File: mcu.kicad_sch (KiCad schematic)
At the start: 17 parts, among them CN1 FTSH-107-01-L-DV-K, U1 STM32H743VITx

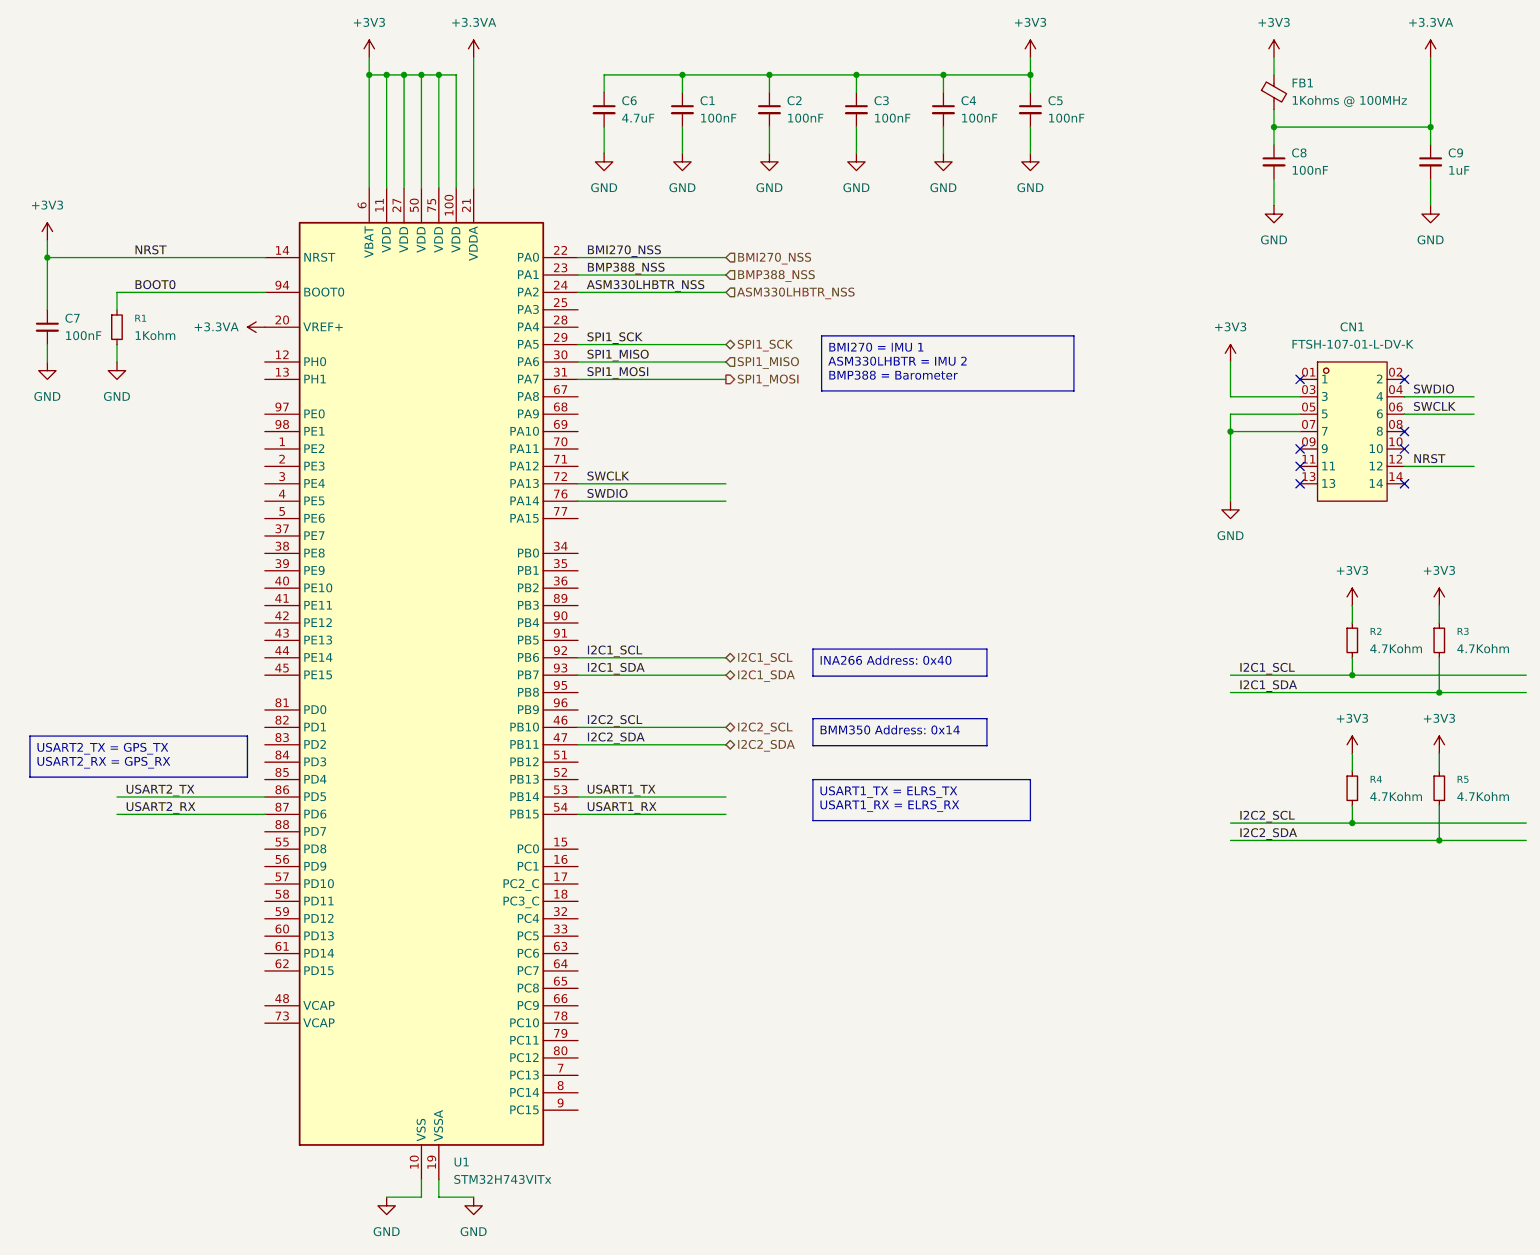
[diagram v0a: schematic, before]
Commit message: Add NavBoard connector and fix Ferrite bead for 3V3A line
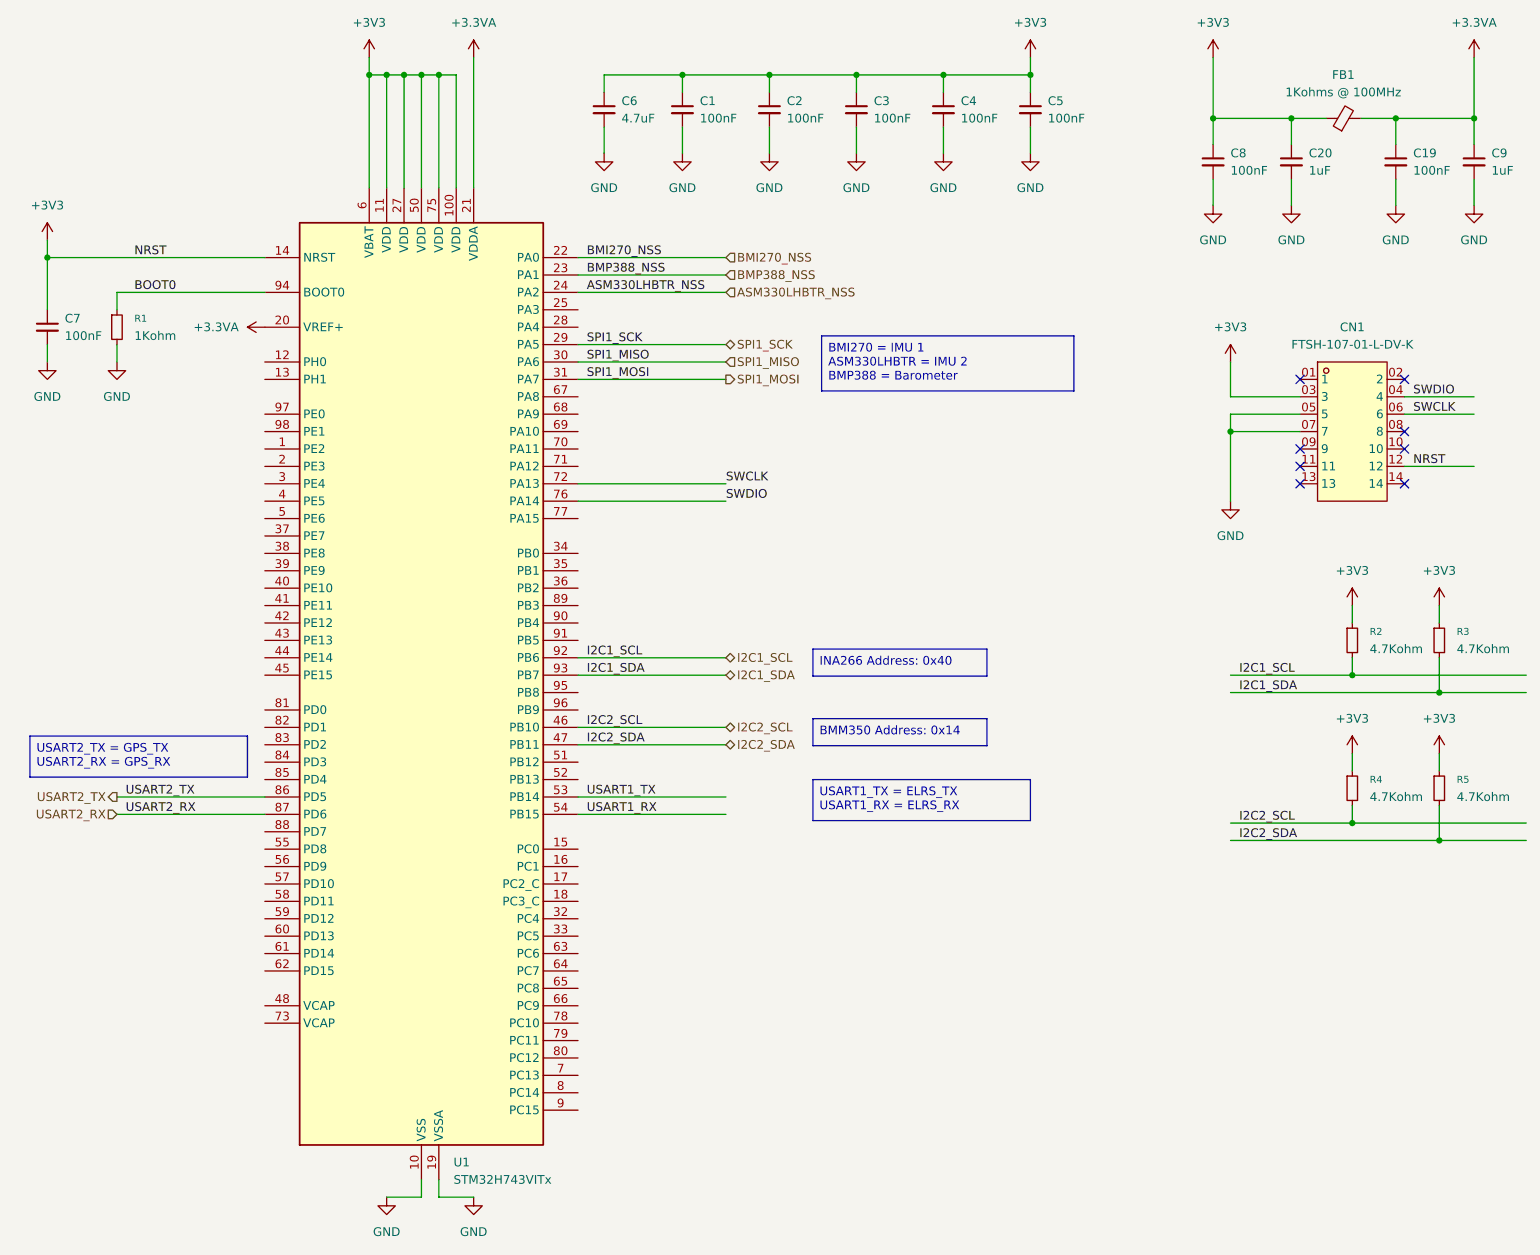
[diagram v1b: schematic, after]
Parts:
- added C19: 100nF, Capacitor_SMD:C_0201_0603Metric_Pad0.64x0.40mm_HandSolder, symbol Device:C_Small
- added C20: 1uF, Capacitor_SMD:C_0201_0603Metric_Pad0.64x0.40mm_HandSolder, symbol Device:C_Small
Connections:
- net +3.3VA: now also C19.1; no longer C8.1
- net +3V3: now also C8.1, C20.1
- net GND: now also C19.2, C20.2
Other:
- moved on the sheet: C8, C9

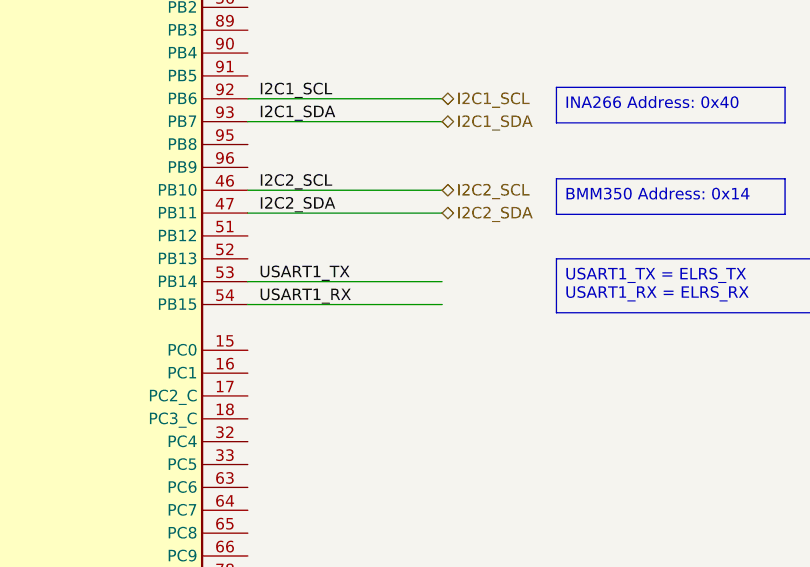
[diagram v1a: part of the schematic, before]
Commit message: added main buck to step Vbat to 5V
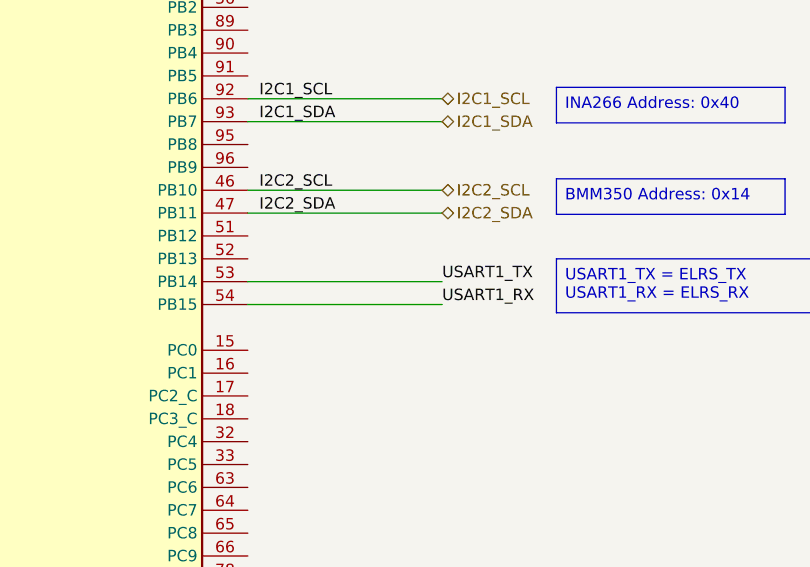
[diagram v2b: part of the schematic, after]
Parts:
- R2, R3, R4, R5: footprint (none) -> Resistor_SMD:R_0201_0603Metric
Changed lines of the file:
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@@
 	)
 	(label "USART1_TX"
-		(at 104.14 129.54 0)
+		(at 124.46 129.54 0)
 		(effects
 			(font
@@
 	)
 	(label "USART1_RX"
-		(at 104.14 132.08 0)
+		(at 124.46 132.08 0)
 		(effects
 			(font
@@
 			)
 		)
-		(property "Footprint" ""
+		(property "Footprint" "Resistor_SMD:R_0201_0603Metric"
 			(at 228.6 106.68 0)
 			(hide yes)
@@
 			)
 		)
-		(property "Footprint" ""
+		(property "Footprint" "Resistor_SMD:R_0201_0603Metric"
 			(at 215.9 106.68 0)
 			(hide yes)
@@
 			)
 		)
-		(property "Footprint" ""
+		(property "Footprint" "Resistor_SMD:R_0201_0603Metric"
 			(at 228.6 128.27 0)
 			(hide yes)
@@
 			)
 		)
-		(property "Footprint" ""
+		(property "Footprint" "Resistor_SMD:R_0201_0603Metric"
 			(at 215.9 128.27 0)
 			(hide yes)

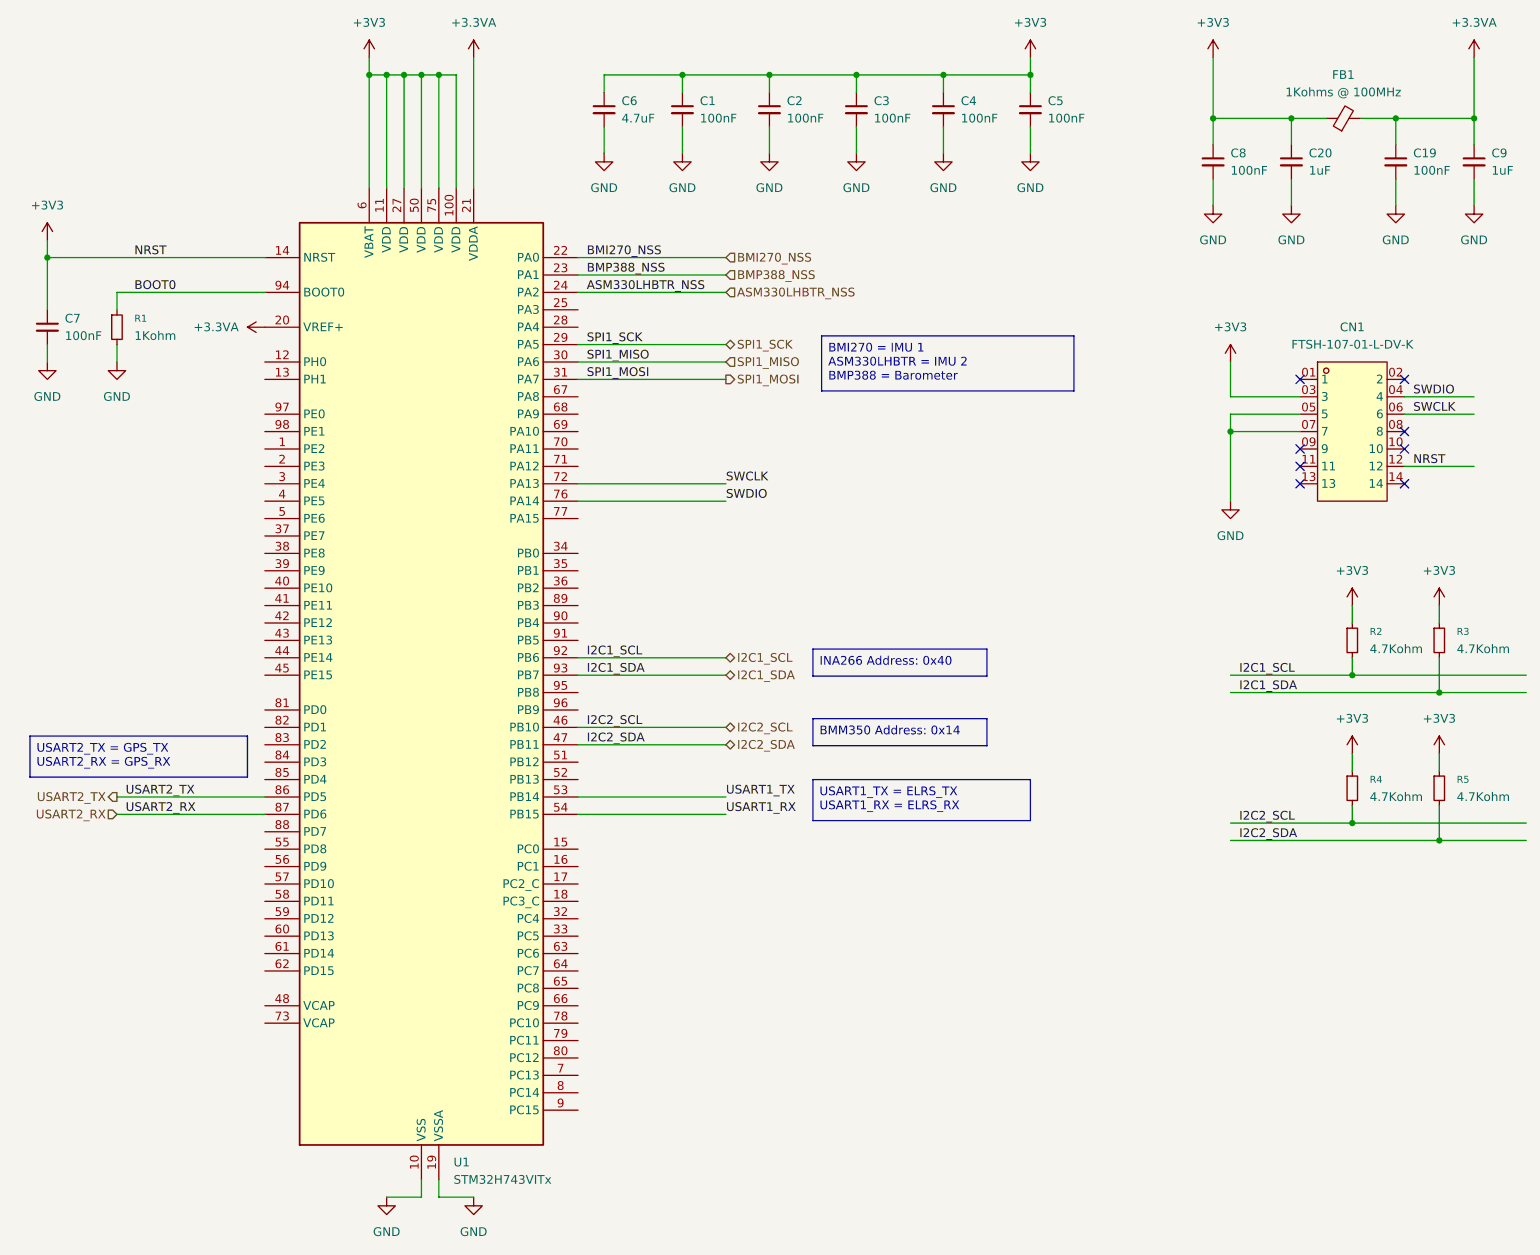
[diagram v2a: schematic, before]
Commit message: mainly added usart 3, uart 4, and I2C3 connections and planning to add a CAN connection
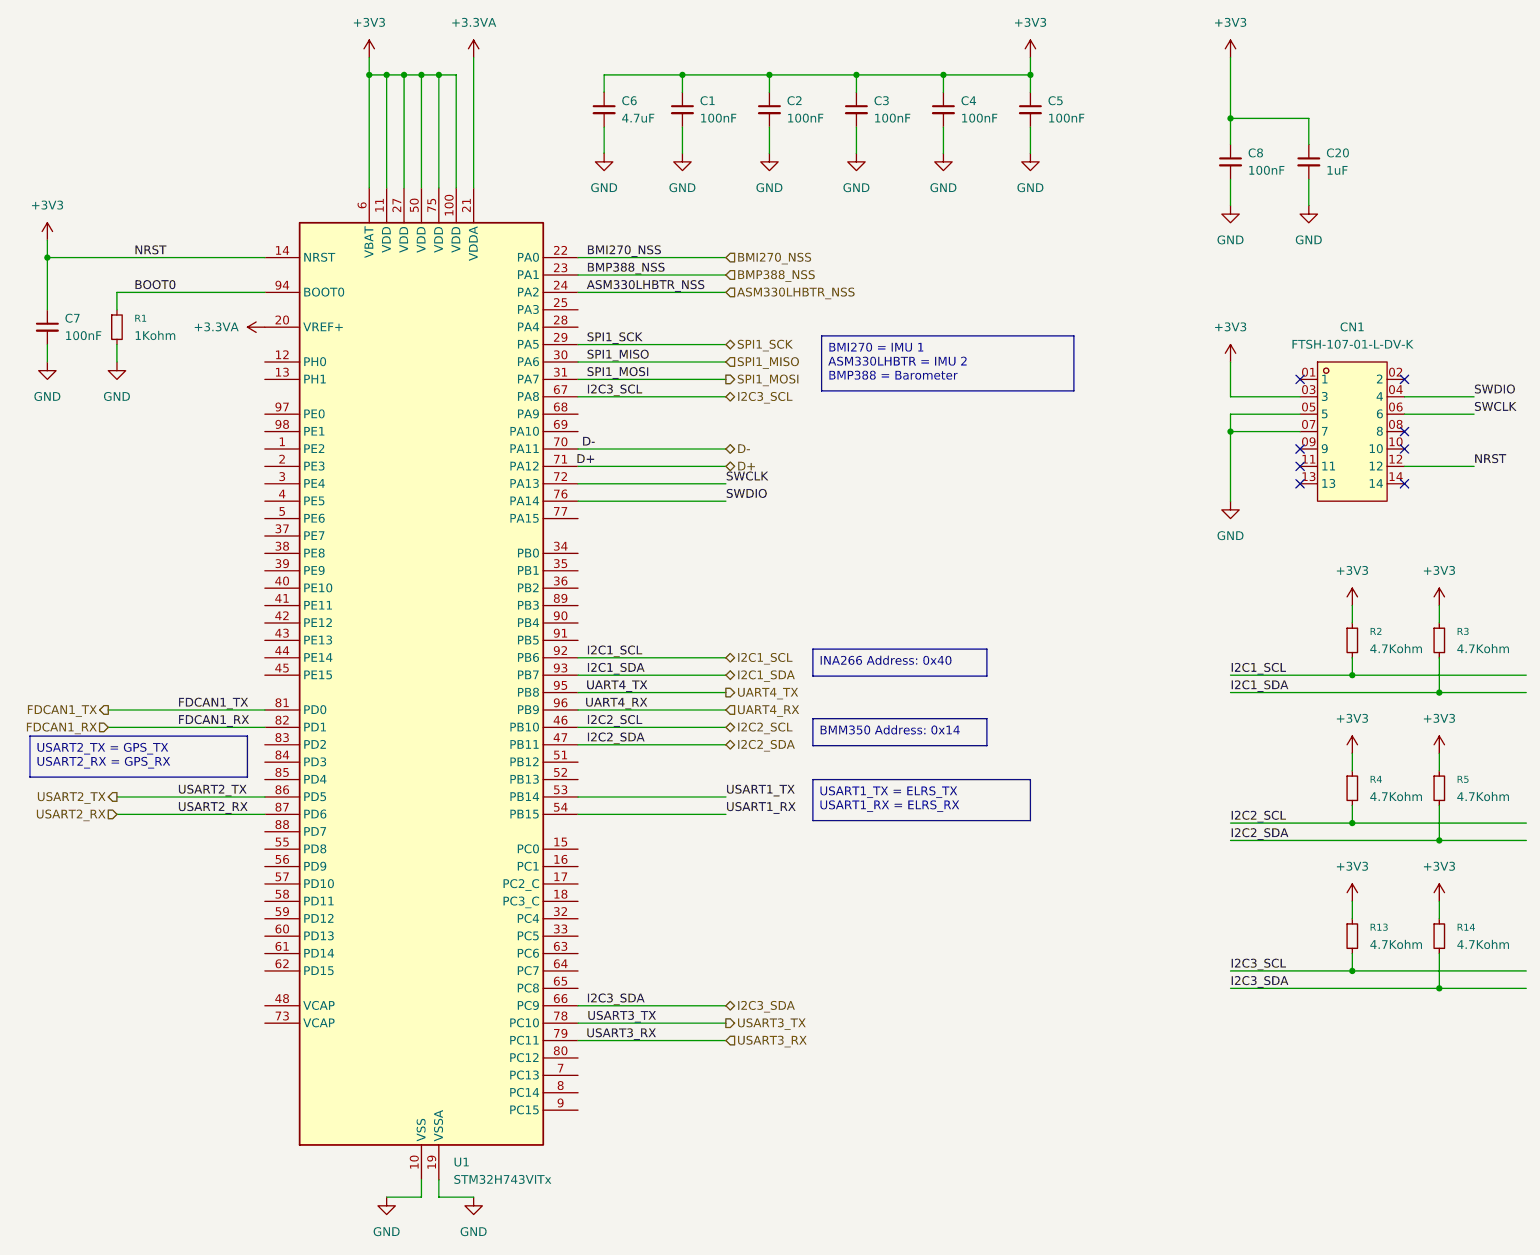
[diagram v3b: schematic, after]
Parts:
- removed C19: 100nF, Capacitor_SMD:C_0201_0603Metric_Pad0.64x0.40mm_HandSolder, symbol Device:C_Small
- removed C9: 1uF, Capacitor_SMD:C_0201_0603Metric_Pad0.64x0.40mm_HandSolder, symbol Device:C_Small
- removed FB1: 1Kohms @ 100MHz, symbol Device:FerriteBead_Small
- added R13, R14: 4.7Kohm, Resistor_SMD:R_0201_0603Metric, symbol Device:R_Small
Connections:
- net +3V3: now also R13.1, R14.1
- net I2C3_SDA: now reaches U1.66 (PC9)
- net I2C3_SDA: now also R14.2
- net I2C3_SCL: now reaches U1.67 (PA8)
- net I2C3_SCL: now also R13.2
- net D-: now reaches U1.70 (PA11)
- net D+: now reaches U1.71 (PA12)
- net USART3_TX: now reaches U1.78 (PC10)
- net USART3_RX: now reaches U1.79 (PC11)
- net FDCAN1_TX: now reaches U1.81 (PD0)
- net FDCAN1_RX: now reaches U1.82 (PD1)
- net UART4_TX: now reaches U1.95 (PB8)
- net UART4_RX: now reaches U1.96 (PB9)
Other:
- moved on the sheet: C20, C8
